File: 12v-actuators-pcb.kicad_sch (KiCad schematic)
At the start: 13 parts, among them J1 12V_C_MOT, J2 3.5mm WR-TBL, J3 690367280676, J4 LCD_DEG, J5 CAN, U1 MCP2551-I-SN, U2 NUCLEO-F303K8

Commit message: Update schematic pinout for LED_EN + Add mechanical constraints to PCB layout
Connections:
- net LED_EN: now also U2.1.15 (PB4); no longer U2.2.5 (PA2)
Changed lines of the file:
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@@
   (no_connect (at 109.22 128.27))
   (no_connect (at 109.22 133.35))
+  (no_connect (at 132.08 135.89))
   (no_connect (at 109.22 130.81))
   (no_connect (at 132.08 130.81))
-  (no_connect (at 109.22 161.29))
   (no_connect (at 132.08 133.35))
   (no_connect (at 111.76 45.72))
@@
     (stroke (width 0) (type default))
   )
-  (wire (pts (xy 132.08 135.89) (xy 142.24 135.89))
+  (wire (pts (xy 109.22 161.29) (xy 99.06 161.29))
     (stroke (width 0) (type default))
   )
@@
     (effects (font (size 1.27 1.27)) (justify left bottom))
   )
-  (label "LED_EN" (at 142.24 135.89 180) (fields_autoplaced)
-    (effects (font (size 1.27 1.27)) (justify right bottom))
+  (label "LED_EN" (at 99.06 161.29 0) (fields_autoplaced)
+    (effects (font (size 1.27 1.27)) (justify left bottom))
   )
   (label "PWR_12V" (at 22.86 33.02 0) (fields_autoplaced)

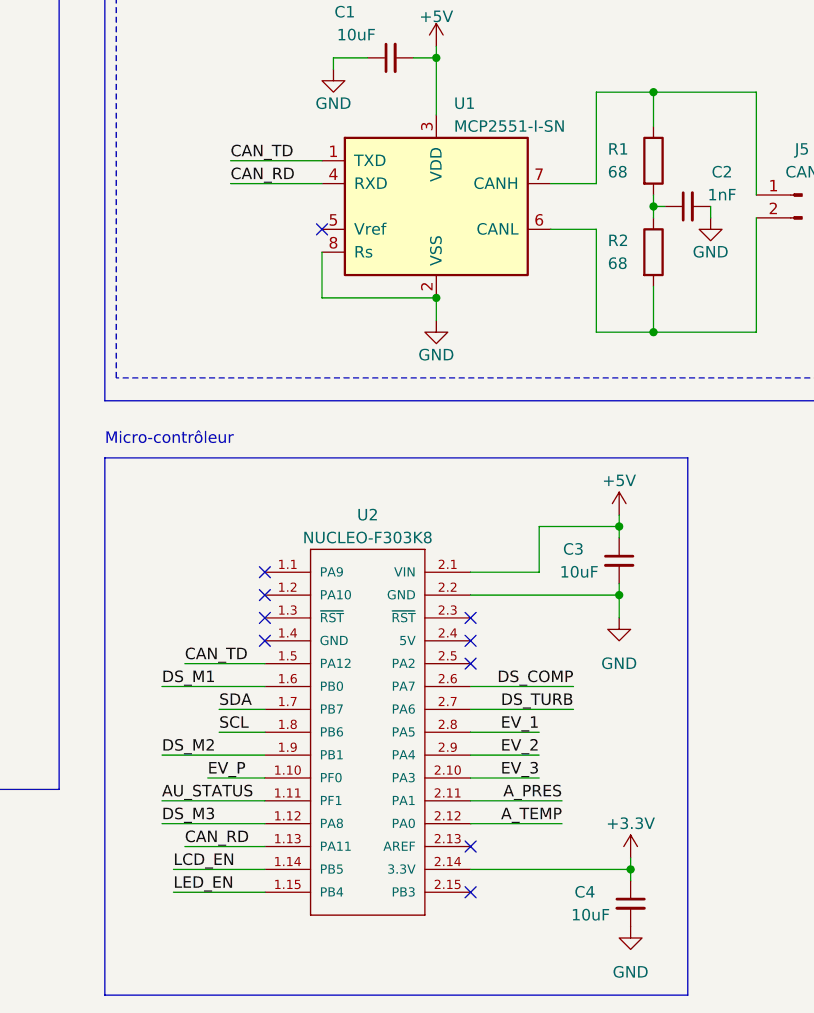
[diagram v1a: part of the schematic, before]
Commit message: Before making power planes
Signal routing done. Added I2C level shifter in schematics.
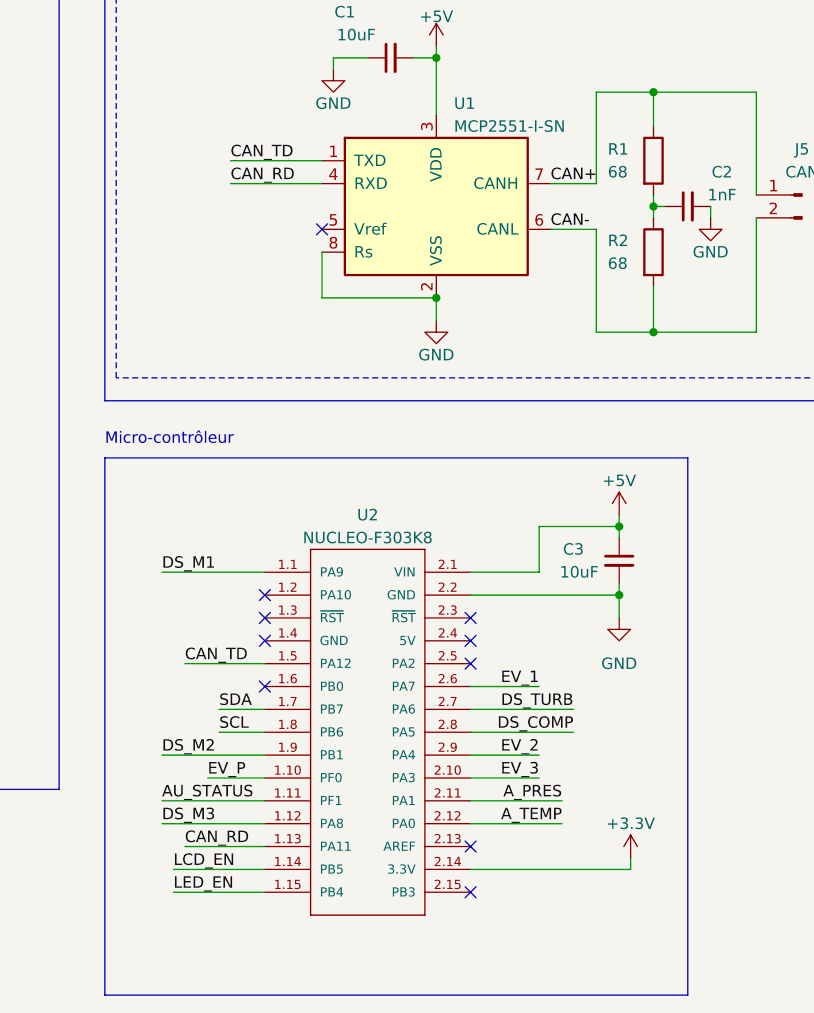
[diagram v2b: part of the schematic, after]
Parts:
- removed C4: 10uF, Capacitor_SMD:C_0805_2012Metric, symbol Device:C_Small
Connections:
- net DS_COMP: now also U2.2.8 (PA5); no longer U2.2.6 (PA7)
- net DS_M1: now also U2.1.1 (PA9); no longer U2.1.6 (PB0)
- net EV_1: now also U2.2.6 (PA7); no longer U2.2.8 (PA5)
- net CAN+: now reaches J5.1 (Pin_1), R1.1, U1.7 (CANH)
- net CAN-: now reaches J5.2 (Pin_2), R2.2, U1.6 (CANL)
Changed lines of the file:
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@@
   (junction (at 163.83 36.83) (diameter 0) (color 0 0 0 0)
   )
-  (junction (at 149.86 158.75) (diameter 0) (color 0 0 0 0)
-  )
   (junction (at 152.4 99.06) (diameter 0) (color 0 0 0 0)
   )
@@
   (junction (at 128.27 95.25) (diameter 0) (color 0 0 0 0)
   )
+  (no_connect (at 109.22 138.43))
   (no_connect (at 121.92 38.1))
   (no_connect (at 115.57 87.63))
@@
   (no_connect (at 132.08 133.35))
   (no_connect (at 111.76 45.72))
-  (no_connect (at 109.22 125.73))
   (no_connect (at 121.92 33.02))
   (wire (pts (xy 24.13 46.99) (xy 36.83 46.99))
@@
     (stroke (width 0) (type default))
   )
+  (wire (pts (xy 97.79 125.73) (xy 109.22 125.73))
+    (stroke (width 0) (type default))
+  )
   (wire (pts (xy 22.86 36.83) (xy 36.83 36.83))
     (stroke (width 0) (type default))
@@
     (stroke (width 0) (type default))
   )
-  (wire (pts (xy 132.08 138.43) (xy 143.51 138.43))
-    (stroke (width 0) (type default))
-  )
   (wire (pts (xy 163.83 86.36) (xy 163.83 99.06))
     (stroke (width 0) (type default))
@@
     (stroke (width 0) (type default))
   )
-  (wire (pts (xy 132.08 143.51) (xy 139.7 143.51))
-    (stroke (width 0) (type default))
-  )
   (wire (pts (xy 146.05 72.39) (xy 152.4 72.39))
     (stroke (width 0) (type default))
@@
     (stroke (width 0) (type default))
   )
+  (wire (pts (xy 132.08 138.43) (xy 139.7 138.43))
+    (stroke (width 0) (type default))
+  )
   (wire (pts (xy 69.85 44.45) (xy 80.01 44.45))
     (stroke (width 0) (type default))
@@
     (stroke (width 0) (type default))
   )
+  (wire (pts (xy 132.08 143.51) (xy 143.51 143.51))
+    (stroke (width 0) (type default))
+  )
   (wire (pts (xy 153.67 31.75) (xy 163.83 31.75))
     (stroke (width 0) (type default))
@@
     (stroke (width 0) (type default))
   )
-  (wire (pts (xy 149.86 160.02) (xy 149.86 158.75))
-    (stroke (width 0) (type default))
-  )
   (wire (pts (xy 25.4 130.81) (xy 36.83 130.81))
     (stroke (width 0) (type default))
@@
     (stroke (width 0) (type default))
   )
-  (wire (pts (xy 97.79 138.43) (xy 109.22 138.43))
-    (stroke (width 0) (type default))
-  )
   (wire (pts (xy 128.27 67.31) (xy 128.27 68.58))
     (stroke (width 0) (type default))
@@
     (effects (font (size 1.27 1.27)) (justify left bottom))
   )
-  (label "DS_M1" (at 97.79 138.43 0) (fields_autoplaced)
-    (effects (font (size 1.27 1.27)) (justify left bottom))
-  )
   (label "EV_2" (at 80.01 40.64 180) (fields_autoplaced)
     (effects (font (size 1.27 1.27)) (justify right bottom))
@@
     (effects (font (size 1.27 1.27)) (justify left bottom))
   )
+  (label "EV_1" (at 139.7 138.43 180) (fields_autoplaced)
+    (effects (font (size 1.27 1.27)) (justify right bottom))
+  )
   (label "VBATT_12V" (at 153.67 31.75 0) (fields_autoplaced)
     (effects (font (size 1.27 1.27)) (justify left bottom))
@@
     (effects (font (size 1.27 1.27)) (justify right bottom))
   )
+  (label "CAN+" (at 140.97 82.55 0) (fields_autoplaced)
+    (effects (font (size 1.27 1.27)) (justify left bottom))
+  )
   (label "LCD_EN" (at 200.66 48.26 0) (fields_autoplaced)
     (effects (font (size 1.27 1.27)) (justify left bottom))
@@
     (effects (font (size 1.27 1.27)) (justify left bottom))
   )
-  (label "AU_STATUS" (at 97.79 151.13 0) (fields_autoplaced)
+  (label "DS_M1" (at 97.79 125.73 0) (fields_autoplaced)
     (effects (font (size 1.27 1.27)) (justify left bottom))
   )
-  (label "DS_COMP" (at 143.51 138.43 180) (fields_autoplaced)
-    (effects (font (size 1.27 1.27)) (justify right bottom))
+  (label "AU_STATUS" (at 97.79 151.13 0) (fields_autoplaced)
+    (effects (font (size 1.27 1.27)) (justify left bottom))
   )
   (label "A_PRES" (at 25.4 118.11 0) (fields_autoplaced)
@@
     (effects (font (size 1.27 1.27)) (justify right bottom))
   )
-  (label "EV_1" (at 139.7 143.51 180) (fields_autoplaced)
-    (effects (font (size 1.27 1.27)) (justify right bottom))
-  )
   (label "DS_M3" (at 97.79 153.67 0) (fields_autoplaced)
     (effects (font (size 1.27 1.27)) (justify left bottom))
   )
+  (label "DS_COMP" (at 143.51 143.51 180) (fields_autoplaced)
+    (effects (font (size 1.27 1.27)) (justify right bottom))
+  )
   (label "DS_TURB" (at 24.13 43.18 0) (fields_autoplaced)
     (effects (font (size 1.27 1.27)) (justify left bottom))
@@
     (effects (font (size 1.27 1.27)) (justify left bottom))
   )
+  (label "CAN-" (at 140.97 87.63 0) (fields_autoplaced)
+    (effects (font (size 1.27 1.27)) (justify left bottom))
+  )
   (symbol (lib_id "ConnectorsEvo:690367280676") (at 116.84 40.64 90) (unit 1)
     (in_bom yes) (on_board yes) (dnp no)
@@
     )
   )
-  (symbol (lib_id "Device:C_Small") (at 149.86 162.56 0) (unit 1)
-    (in_bom yes) (on_board yes) (dnp no)
-    (property "Reference" "C4" (at 144.78 161.29 0)
-      (effects (font (size 1.27 1.27)))
-    )
-    (property "Value" "10uF" (at 145.415 163.83 0)
-      (effects (font (size 1.27 1.27)))
-    )
-    (property "Footprint" "Capacitor_SMD:C_0805_2012Metric" (at 149.86 162.56 0)
-      (effects (font (size 1.27 1.27)) hide)
-    )
-    (property "Datasheet" "~" (at 149.86 162.56 0)
-      (effects (font (size 1.27 1.27)) hide)
-    )
-    (pin "1")
-    (pin "2")
-    (instances
-      (project "12v-actuators-pcb"
-        (path "/d0b6cc72-ff07-4f5e-a148-04b65c86a715"
-          (reference "C4") (unit 1)
-        )
-      )
-    )
-  )
   (symbol (lib_id "Device:C_Small") (at 156.21 85.09 90) (unit 1)
     (in_bom yes) (on_board yes) (dnp no)
@@
     )
   )
-  (symbol (lib_id "power:GND") (at 149.86 165.1 0) (unit 1)
-    (in_bom yes) (on_board yes) (dnp no) (fields_autoplaced)
-    (property "Reference" "#PWR013" (at 149.86 171.45 0)
-      (effects (font (size 1.27 1.27)) hide)
-    )
-    (property "Value" "GND" (at 149.86 170.18 0)
-      (effects (font (size 1.27 1.27)))
-    )
-    (property "Footprint" "" (at 149.86 165.1 0)
-      (effects (font (size 1.27 1.27)) hide)
-    )
-    (property "Datasheet" "" (at 149.86 165.1 0)
-      (effects (font (size 1.27 1.27)) hide)
-    )
-    (pin "1")
-    (instances
-      (project "12v-actuators-pcb"
-        (path "/d0b6cc72-ff07-4f5e-a148-04b65c86a715"
-          (reference "#PWR013") (unit 1)
-        )
-      )
-    )
-  )
   (symbol (lib_id "power:GNDPWR") (at 199.39 31.75 0) (unit 1)
     (in_bom yes) (on_board yes) (dnp no)
@@
       (effects (font (size 1.27 1.27)) (justify left bottom) hide)
     )
-    (property "Datasheet" "https://www.st.com/resource/en/datasheet/stm32f303k8.pdf" (at 151.13 129.54 0)
+    (property "Datasheet" "ST Microelectronics" (at 151.13 129.54 0)
       (effects (font (size 1.27 1.27)) (justify left bottom) hide)
     )

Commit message: CDR 2025 version WIP
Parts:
- removed C3: 10uF, Capacitor_SMD:C_0805_2012Metric, symbol Device:C_Small
- removed J1: 12V_C_MOT, ConnectorsEvo:691321100002, symbol Connector:Screw_Terminal_01x02
- removed J4: LCD_DEG, Connector_PinHeader_2.54mm:PinHeader_1x03_P2.54mm_Vertical, symbol Connector:Conn_01x03_Pin
- removed J5: CAN, Connector_PinHeader_2.54mm:PinHeader_1x02_P2.54mm_Vertical, symbol Connector:Conn_01x02_Pin
- removed U2: NUCLEO-F303K8, ComponentsEvo:MODULE_NUCLEO-F303K8, symbol ComponentsEvo:NUCLEO-F303K8
- added J5: USB_B_Mini, ConnectorsEvo:USB_Mini-B_Wuerth_65100516121_Horizontal, symbol Connector:USB_B_Mini
- added J8: CAN, Connector_PinHeader_2.54mm:PinHeader_1x03_P2.54mm_Vertical, symbol Connector:Conn_01x03_Pin
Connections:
- net +5V: no longer C1.2, U1.3 (VDD)
- net CAN+: now also J8.1 (Pin_1)
- net CAN-: now also J8.2 (Pin_2)
- net GND: now also J5.5 (GND), J5.6 (Shield)
- net CAN_RD renamed CAN_RX
- net CAN_TD renamed CAN_TX
- new net +5VL: C1.2, U1.3 (VDD)
- new net 5V_CAN: J8.3 (Pin_3)
- new net 5V_USB: J5.1 (VBUS)
- new net USB_DN: J5.2 (D-)
- new net USB_DP: J5.3 (D+)
- no-connect marks 13 -> 5
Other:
- added sheet Alims (Alims.kicad_sch)
- added sheet MCU (mcu.kicad_sch)
- sheet Actionneurs ports: added DATA_LED, EV_10, EV_11, EV_4, EV_5, EV_6, EV_7, EV_8, EV_9, VAC, VBAT_12V; removed DS_M1, DS_M2, DS_M3, LED_EN, VBATT_12V
- sheet Arrêt d'urgence ports: added VBAT_12V; removed VBATT_12V
- sheet Capteurs ports: added none; removed A_PRES
- note removed: "Micro-contrôleur"

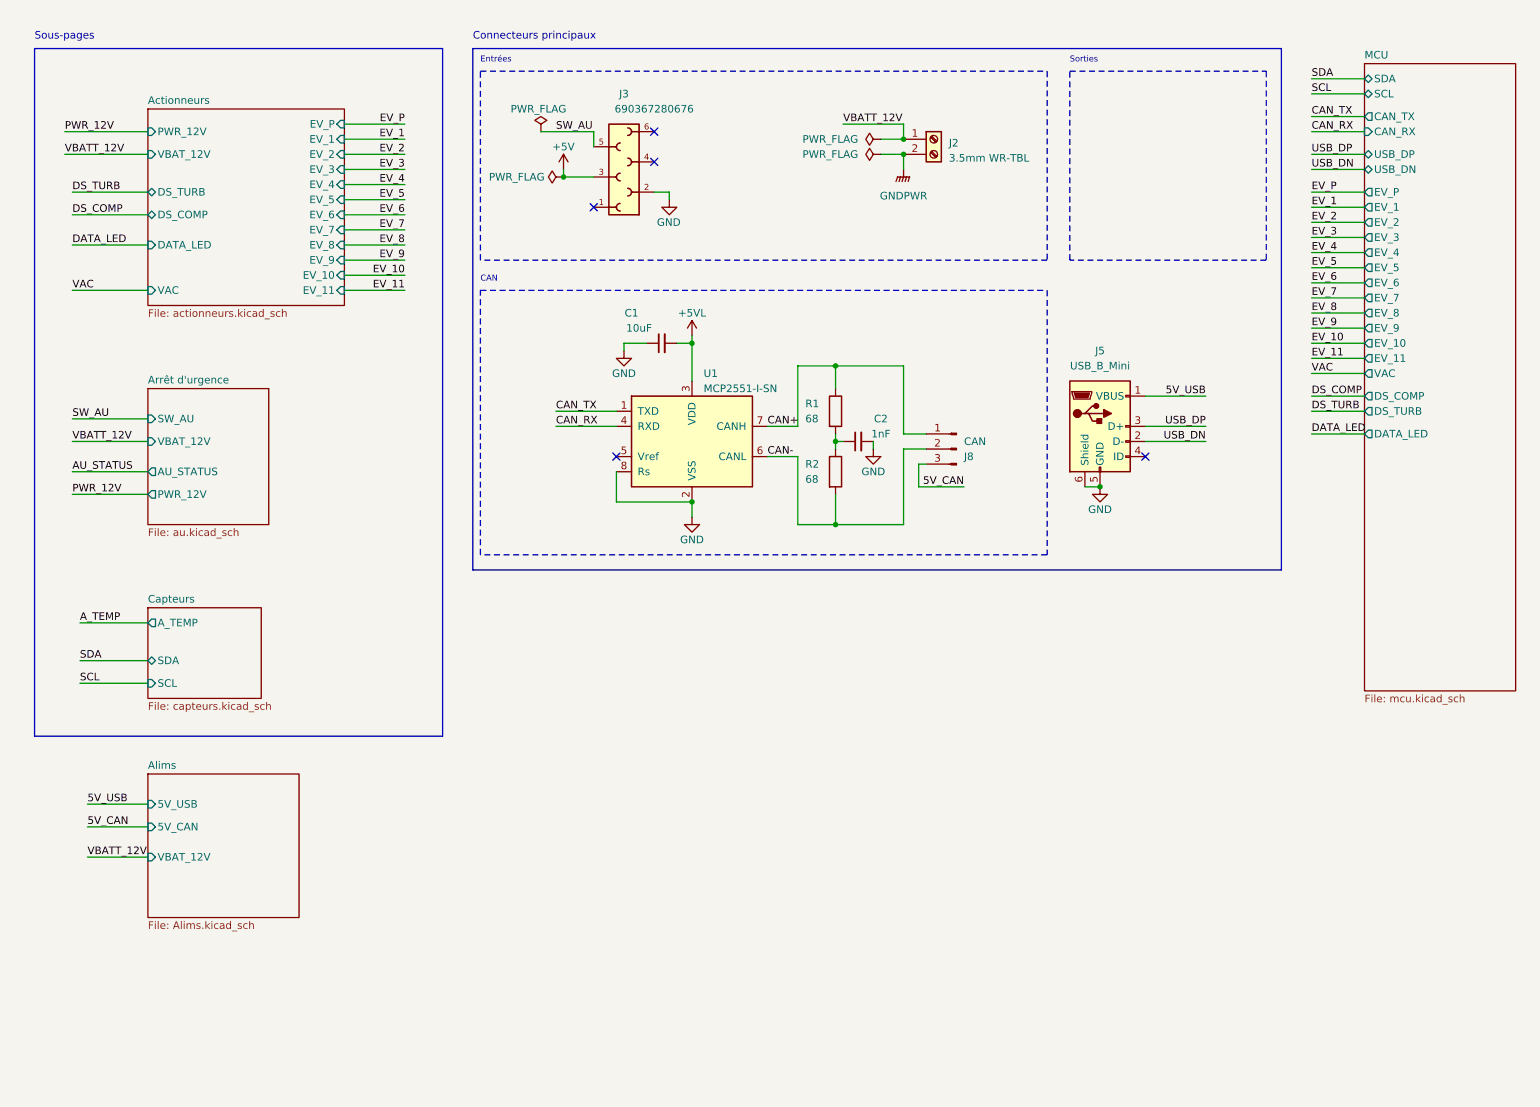
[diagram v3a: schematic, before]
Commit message: Simplification arborescence schema, correction duplicate designator TODO: connect floating signal on MCU sheet, update routing, split the board in two
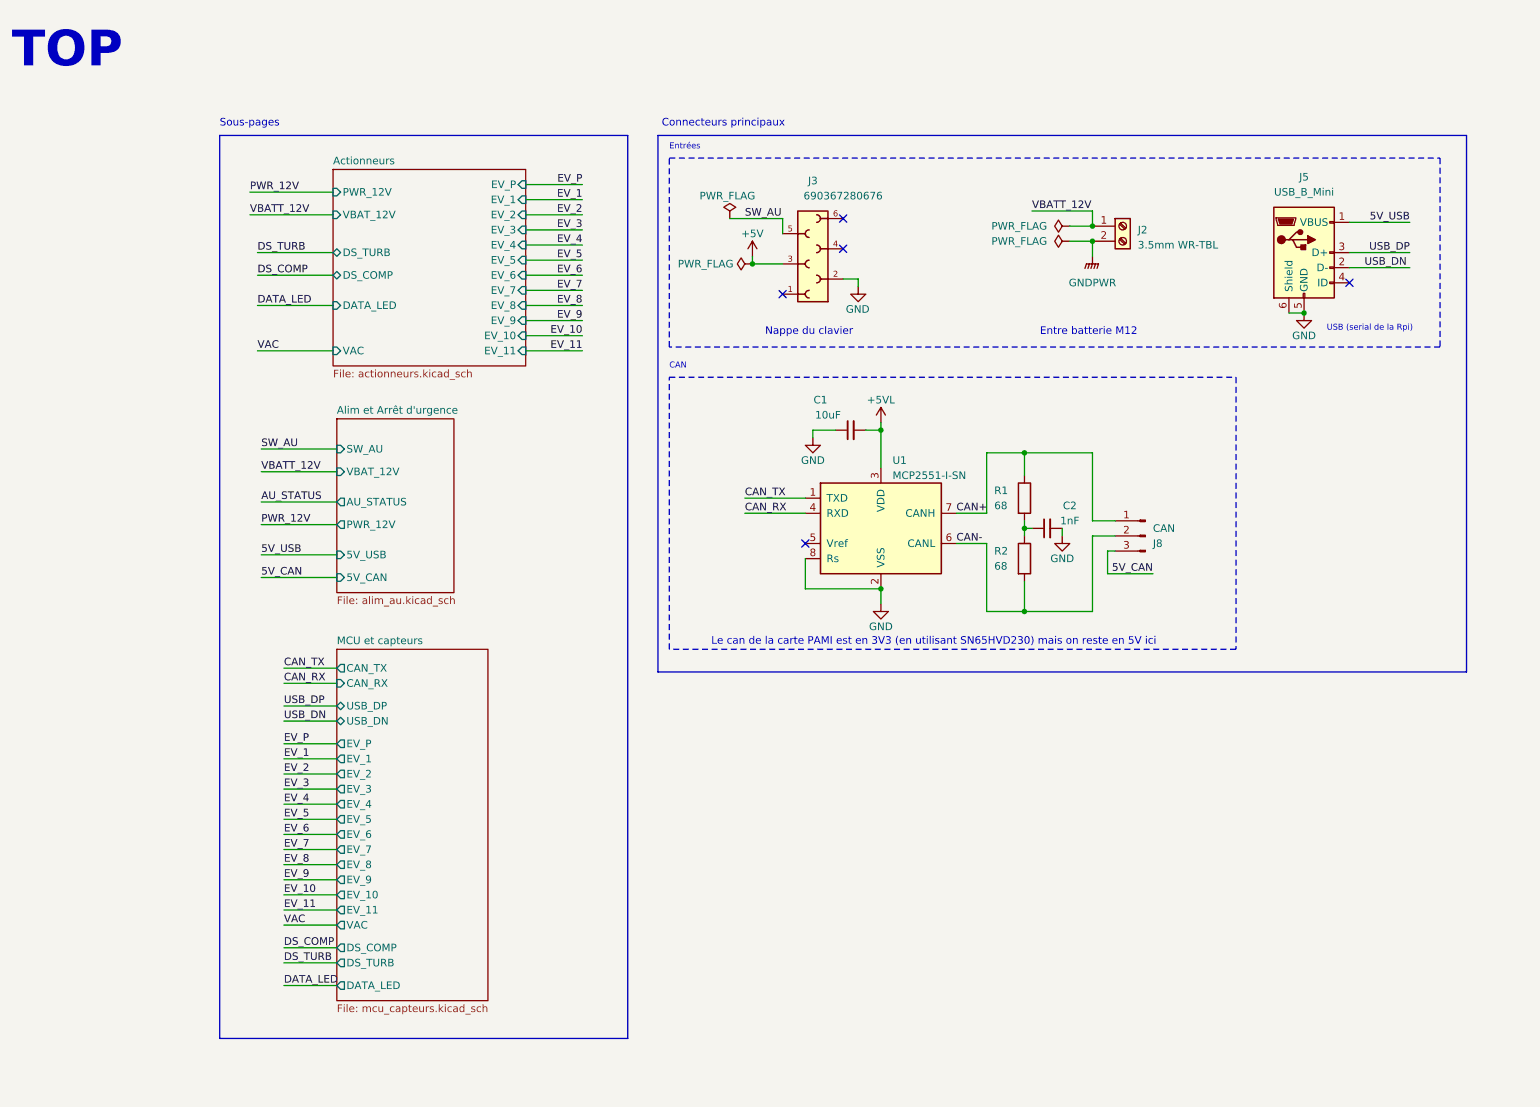
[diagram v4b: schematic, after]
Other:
- sheet Arrêt d'urgence renamed Alim et Arrêt d'urgence
- removed sheet Alims
- removed sheet Capteurs
- removed sheet MCU
- added sheet MCU et capteurs (mcu_capteurs.kicad_sch)
- sheet Alim et Arrêt d'urgence: file au.kicad_sch -> alim_au.kicad_sch
- sheet Alim et Arrêt d'urgence ports: added 5V_CAN, 5V_USB; removed none
- note added: "Entre batterie M12"
- note added: "Le can de la carte PAMI est en 3V3 (en utilisant SN65HVD230) mais on reste en 5V ici"
- note added: "Nappe du clavier"
- note added: "TOP"
- note added: "USB (serial de la Rpi)"
- note removed: "Sorties"
- title: Carte pneumatique -> Carte pneumatique -TOP
- moved on the sheet: C1, C2, J2, J3, J5, J8, R1, R2, U1
